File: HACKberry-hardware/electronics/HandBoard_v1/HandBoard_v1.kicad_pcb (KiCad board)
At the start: 2 copper layers, 60.8 x 54.8 mm, 12 parts, among them CON1 BARREL_JACK_MJ179PH, SW1:MAX1 SW_PUSH_SKRGAQD010, SW2:MIN1 SW_PUSH_SKRGAQD010, SW3:Thumb1 SW_PUSH_SKRGAQD010, SW4:Middle1 SW_PUSH_SKRGAQD010, SW5 SWITCH_SS-12SDP2, U1 3-CONDUCTOR_MINIATUIRE_JACK_M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, U2 Arduino_Micro, U3 Seed_Studio_Adjustable_DC/DC_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, U4 Servo_Motor_S03N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

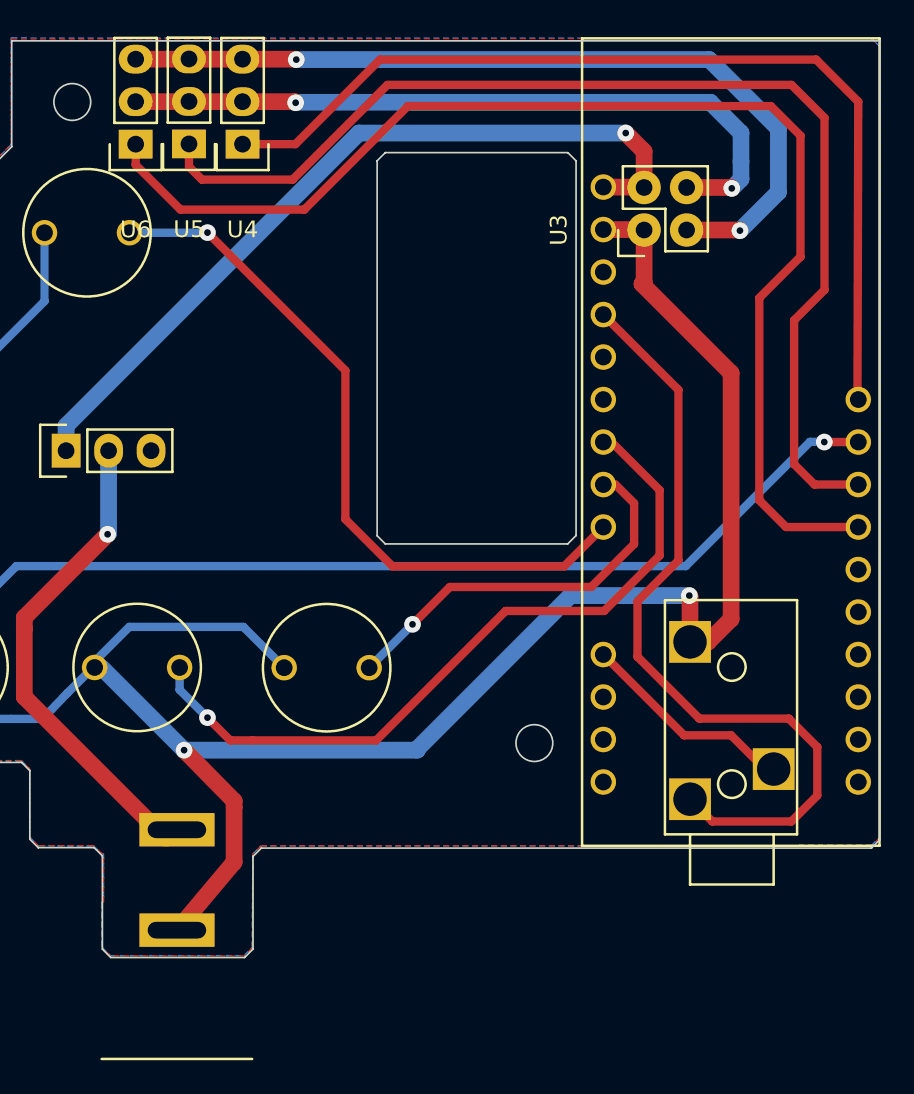
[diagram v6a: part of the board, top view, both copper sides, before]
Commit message: Updated the PCB files for PCB manufacturing service.
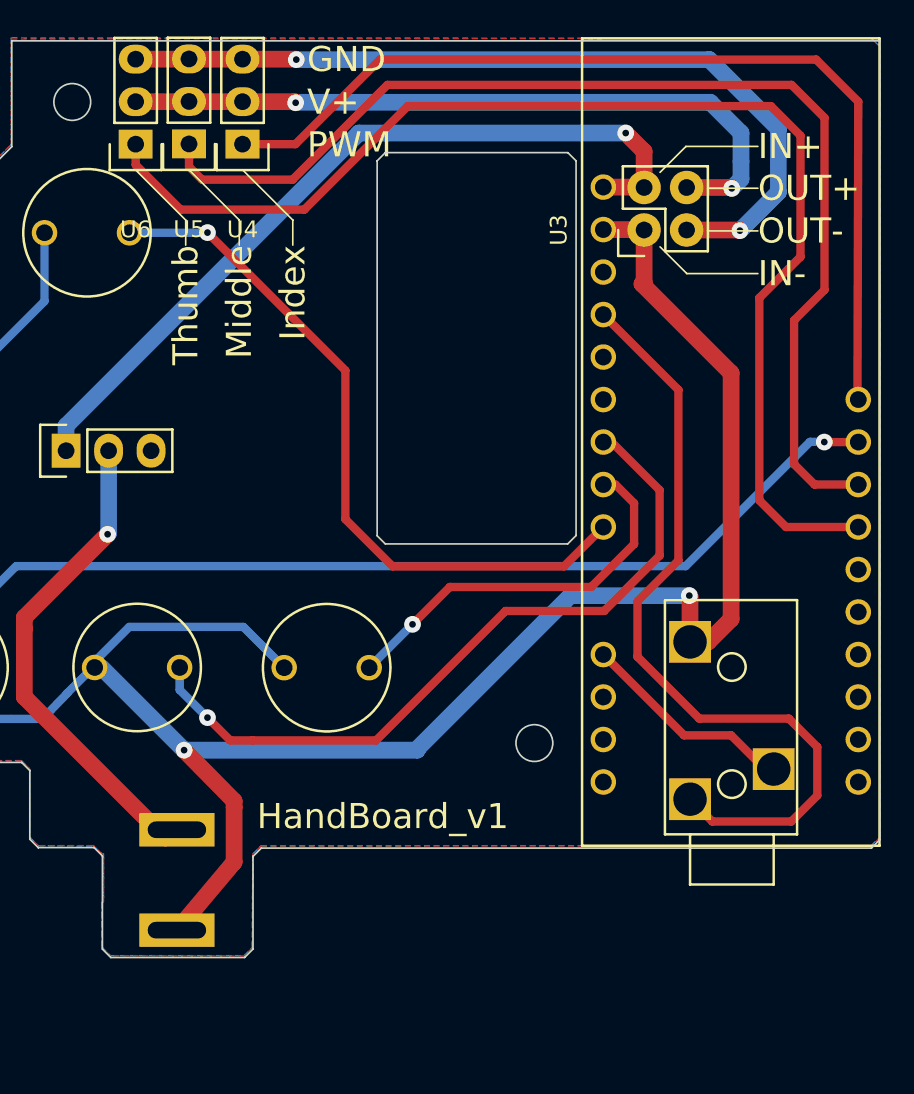
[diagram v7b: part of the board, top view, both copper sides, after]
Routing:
- net Net-(U2-Pad5V): track 20.0 -> 6.36 mm
- net Net-(U1-Pad2): track 28.0 -> 41.7 mm
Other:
- board text added: "GND"
- board text added: "HandBoard_v1"
- board text added: "IN+"
- board text added: "IN-"
- board text added: "Index"
- board text added: "Middle"
- board text added: "OUT+"
- board text added: "OUT-"
- board text added: "PWM"
- board text added: "Thumb"
- board text added: "V+"
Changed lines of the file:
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@@
-(kicad_pcb (version 4) (host pcbnew "(after 2015-may-01 BZR unknown)-product")
+(kicad_pcb (version 4) (host pcbnew 4.0.1-stable)
   (general
     (links 22)
     (no_connects 3)
-    (area 87.427524 80.110499 171.030076 142.32932)
+    (area 95.268 66.530187 157.666101 142.916076)
     (thickness 1.6)
-    (drawings 32)
+    (drawings 55)
     (tracks 159)
     (zones 0)
@@
       (layerselection 0x010f0_80000001)
       (usegerberextensions true)
-      (usegerberattributes true)
       (excludeedgelayer true)
       (linewidth 0.100000)
@@
       (viasonmask false)
       (mode 1)
-      (useauxorigin true)
+      (useauxorigin false)
       (hpglpennumber 1)
       (hpglpenspeed 20)
@@
       (plotinvisibletext false)
       (padsonsilk false)
-      (subtractmaskfromsilk true)
+      (subtractmaskfromsilk false)
       (outputformat 1)
       (mirror false)
       (drillshape 0)
       (scaleselection 1)
-      (outputdirectory ../../../../../../Desktop/151120HandBoard/))
+      (outputdirectory 160111HandBoard_v1_2/))
   )
   (net 0 "")
@@
     (uvia_drill 0.1)
   )
+  (module HACKberry_v1:MJ179PH (layer F.Cu)
+    (at 115.39474 141.87932 90)
+    (fp_text reference CON1 (at 13.7 3.75 90) (layer F.SilkS) hide
+      (effects (font (size 1 1) (thickness 0.15)))
+    )
+    (fp_text value BARREL_JACK_MJ179PH (at 13.5 -7.25 90) (layer F.Fab)
+      (effects (font (size 1 1) (thickness 0.15)))
+    )
+    (pad "" thru_hole rect (at 7.7 0 90) (size 2 4.5) (drill oval 1 3.5) (layers *.Cu *.Mask F.SilkS))
+    (pad "" thru_hole rect (at 13.7 0 90) (size 2 4.5) (drill oval 1 3.5) (layers *.Cu *.Mask F.SilkS))
+  )
   (module Pin_Headers:Pin_Header_Straight_2x02 (layer F.Cu)
     (at 143.3195 92.329 90)
@@
       (net 19 "Net-(U2-Pad12)"))
   )
-  (module HACKberry_v1:MJ179PH (layer F.Cu)
-    (at 115.39474 141.87932 90)
-    (fp_text reference CON1 (at 13.7 3.75 90) (layer F.SilkS) hide
-      (effects (font (size 1 1) (thickness 0.15)))
-    )
-    (fp_text value BARREL_JACK_MJ179PH (at 13.5 -7.25 90) (layer F.Fab)
-      (effects (font (size 1 1) (thickness 0.15)))
-    )
-    (fp_line (start 0 -4.5) (end 0 4.5) (layer F.SilkS) (width 0.15))
-    (pad "" thru_hole rect (at 7.7 0 90) (size 2 4.5) (drill oval 1 3.5) (layers *.Cu *.Mask F.SilkS))
-    (pad "" thru_hole rect (at 13.7 0 90) (size 2 4.5) (drill oval 1 3.5) (layers *.Cu *.Mask F.SilkS))
-  )
   (module HACKberry_v1:MINIATURE_JACK_MJ-4535-3 (layer F.Cu)
     (at 148.5646 125.4506 270)
@@
     )
   )
+  (gr_text HandBoard_v1 (at 120.1711 127.3836) (layer F.SilkS)
+    (effects (font (size 1.5 1.5) (thickness 0.3)) (justify left))
+  )
+  (gr_text IN- (at 150.1211 94.9336) (layer F.SilkS)
+    (effects (font (size 1.5 1.5) (thickness 0.3)) (justify left))
+  )
+  (gr_text PWM (at 123.1711 87.2336) (layer F.SilkS)
+    (effects (font (size 1.5 1.5) (thickness 0.3)) (justify left))
+  )
+  (gr_text V+ (at 123.1711 84.6836) (layer F.SilkS)
+    (effects (font (size 1.5 1.5) (thickness 0.3)) (justify left))
+  )
+  (gr_text GND (at 123.1711 82.1336) (layer F.SilkS)
+    (effects (font (size 1.5 1.5) (thickness 0.3)) (justify left))
+  )
+  (gr_text IN+ (at 150.1211 87.3336) (layer F.SilkS)
+    (effects (font (size 1.5 1.5) (thickness 0.3)) (justify left))
+  )
+  (gr_line (start 145.8711 94.9336) (end 144.2711 93.3336) (angle 90) (layer F.SilkS) (width 0.1))
+  (gr_line (start 150.1211 94.9336) (end 145.8711 94.9336) (angle 90) (layer F.SilkS) (width 0.1))
+  (gr_line (start 145.8211 87.3336) (end 144.2711 88.8836) (angle 90) (layer F.SilkS) (width 0.1))
+  (gr_line (start 150.1211 87.3336) (end 145.8211 87.3336) (angle 90) (layer F.SilkS) (width 0.1))
+  (gr_text OUT- (at 150.1211 92.3836) (layer F.SilkS)
+    (effects (font (size 1.5 1.5) (thickness 0.3)) (justify left))
+  )
+  (gr_text OUT+ (at 150.1211 89.8336) (layer F.SilkS)
+    (effects (font (size 1.5 1.5) (thickness 0.3)) (justify left))
+  )
+  (gr_line (start 147.1211 92.3836) (end 150.1211 92.3836) (angle 90) (layer F.SilkS) (width 0.1))
+  (gr_line (start 147.1211 89.8336) (end 150.1211 89.8336) (angle 90) (layer F.SilkS) (width 0.1))
+  (gr_text Index (at 122.3211 93.2336 90) (layer F.SilkS)
+    (effects (font (size 1.5 1.5) (thickness 0.3)) (justify right))
+  )
+  (gr_text Middle (at 119.1211 93.2336 90) (layer F.SilkS)
+    (effects (font (size 1.5 1.5) (thickness 0.3)) (justify right))
+  )
+  (gr_text Thumb (at 115.9211 93.2336 90) (layer F.SilkS)
+    (effects (font (size 1.5 1.5) (thickness 0.3)) (justify right))
+  )
+  (gr_line (start 122.3211 91.7336) (end 122.3211 93.2336) (angle 90) (layer F.SilkS) (width 0.1))
+  (gr_line (start 119.1211 91.7336) (end 119.1211 93.2336) (angle 90) (layer F.SilkS) (width 0.1))
+  (gr_line (start 119.3211 88.7336) (end 122.3211 91.7336) (angle 90) (layer F.SilkS) (width 0.1))
+  (gr_line (start 116.1211 88.7336) (end 119.1211 91.7336) (angle 90) (layer F.SilkS) (width 0.1))
+  (gr_line (start 115.9211 91.7336) (end 115.9211 93.2336) (angle 90) (layer F.SilkS) (width 0.1))
+  (gr_line (start 112.9211 88.7336) (end 115.9211 91.7336) (angle 90) (layer F.SilkS) (width 0.1))
   (gr_line (start 119.9411 129.7736) (end 119.9411 135.3136) (angle 90) (layer Edge.Cuts) (width 0.1))
   (gr_line (start 111.4411 135.8136) (end 119.4411 135.8136) (angle 90) (layer Edge.Cuts) (width 0.1))
@@
   (segment (start 142.9211 117.8336) (end 146.6211 121.5336) (width 0.5) (layer F.Cu) (net 6))
   (segment (start 142.9211 114.5336) (end 142.9211 117.8336) (width 0.5) (layer F.Cu) (net 6))
+  (segment (start 145.3711 112.0836) (end 142.9211 114.5336) (width 0.5) (layer F.Cu) (net 6))
+  (segment (start 145.3711 101.8836) (end 145.3711 112.0836) (width 0.5) (layer F.Cu) (net 6))
   (segment (start 140.8811 92.3036) (end 143.2941 92.3036) (width 1) (layer F.Cu) (net 7))
   (segment (start 140.8811 97.3836) (end 140.8811 97.3936) (width 0.5) (layer F.Cu) (net 9))
   (segment (start 140.8811 97.3936) (end 145.3711 101.8836) (width 0.5) (layer F.Cu) (net 9))
-  (segment (start 145.3711 101.8836) (end 145.3711 112.0836) (width 0.5) (layer F.Cu) (net 9))
-  (segment (start 145.3711 112.0836) (end 142.9211 114.5336) (width 0.5) (layer F.Cu) (net 9))
   (segment (start 122.4788 87.1982) (end 127.5334 82.1436) (width 0.5) (layer F.Cu) (net 12))
   (segment (start 156.1211 84.6582) (end 156.0711 102.5836) (width 0.5) (layer F.Cu) (net 12) (status 20))

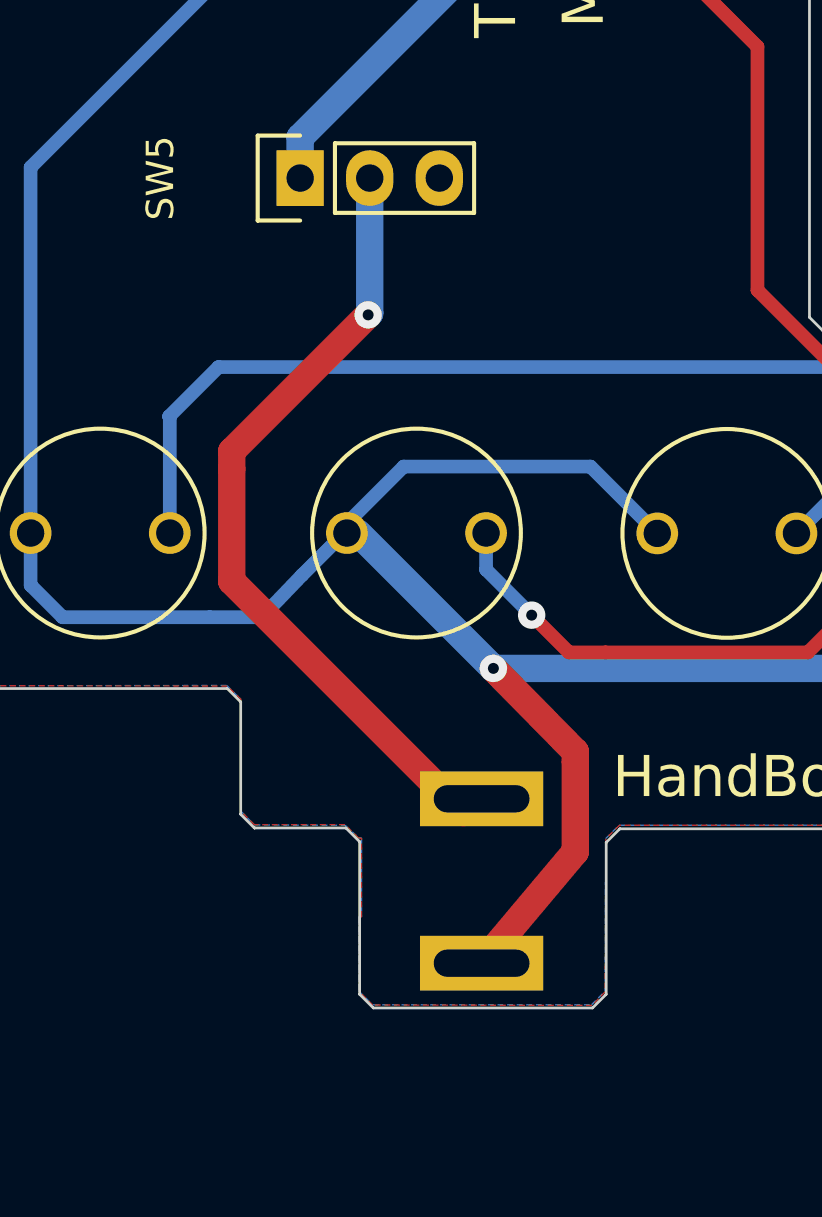
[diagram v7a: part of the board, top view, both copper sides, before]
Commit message: Change DC-jack to PJ-102A
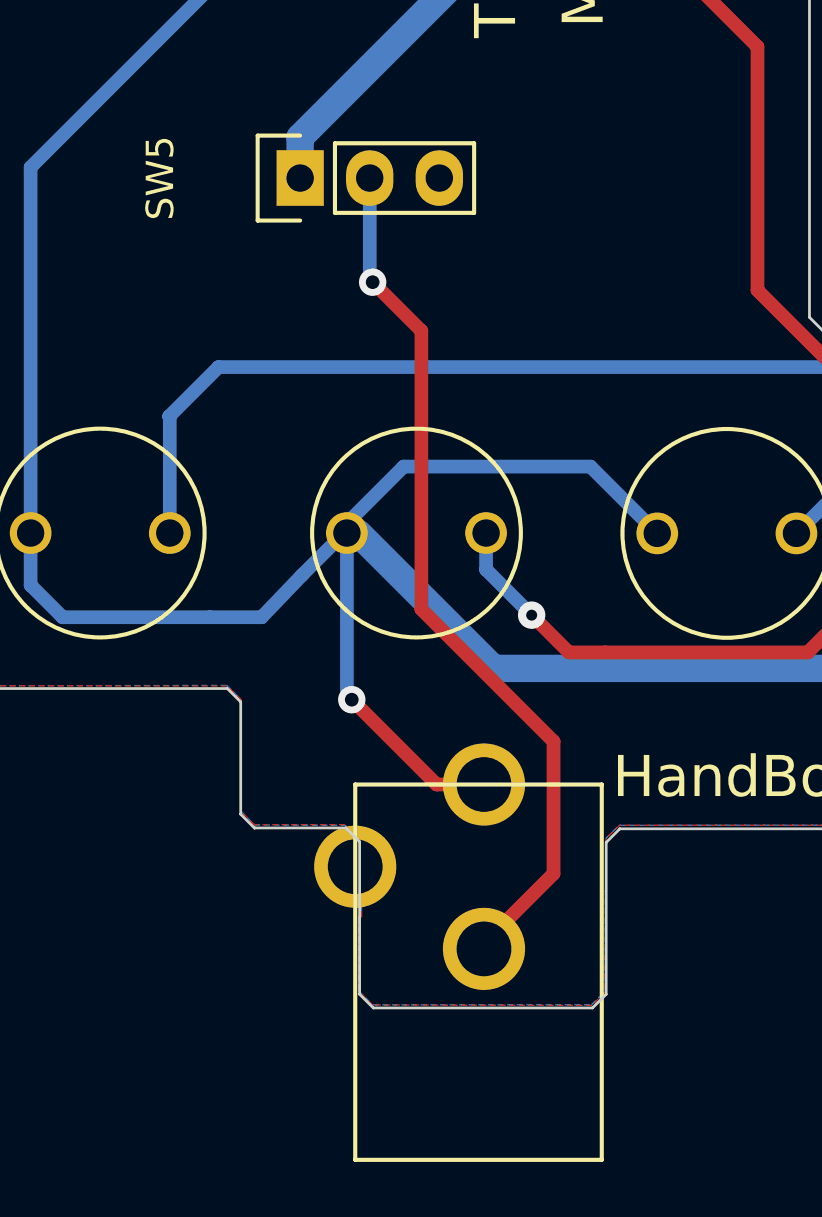
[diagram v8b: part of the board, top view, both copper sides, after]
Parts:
- CON1: value BARREL_JACK_MJ179PH -> BARREL_JACK; footprint HACKberry_v1:MJ179PH -> HACKberry_v1:PJ-102A
- U1: value 3-CONDUCTOR_MINIATUIRE_JACK_MJ-4535-3 -> 3-CONDUCTOR_MINIATUIRE_JACK_MJ-4535-3-RESCUE-HandBoard_v1
- U5, U6: value Servo_Motor_MG90S -> Servo_Motor_ES08MD
- moved CON1 11.2 mm to (115.5, 130.7), turned to 0 degrees
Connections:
- SW1:MAX1 pad 1: Net-(CON1-Pad3) -> Net-(CON1-Pad2)
- SW2:MIN1 pad 1: Net-(CON1-Pad3) -> Net-(CON1-Pad2)
- SW3:Thumb1 pad 1: Net-(CON1-Pad3) -> Net-(CON1-Pad2)
- SW4:Middle1 pad 1: Net-(CON1-Pad3) -> Net-(CON1-Pad2)
- U1 pad 1: Net-(CON1-Pad3) -> Net-(CON1-Pad2)
- U2 pad GND: Net-(U2-PadGND) -> Net-(CON1-Pad2)
- U2 pad eRST: Net-(U2-PadRST) -> (no net)
- U3 pad 2: Net-(CON1-Pad3) -> Net-(CON1-Pad2)
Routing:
- net Net-(CON1-Pad2): track 0.00 -> 145.8 mm, vias 0 -> 2
- net Net-(CON1-Pad3): track 144.4 -> 0.00 mm, vias 2 -> 0
- net Net-(CON1-Pad1): track 28.8 -> 32.0 mm
- net Net-(U2-PadGND): track 2.41 -> 0.00 mm
